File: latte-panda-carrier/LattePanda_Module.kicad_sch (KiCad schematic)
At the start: 9 parts

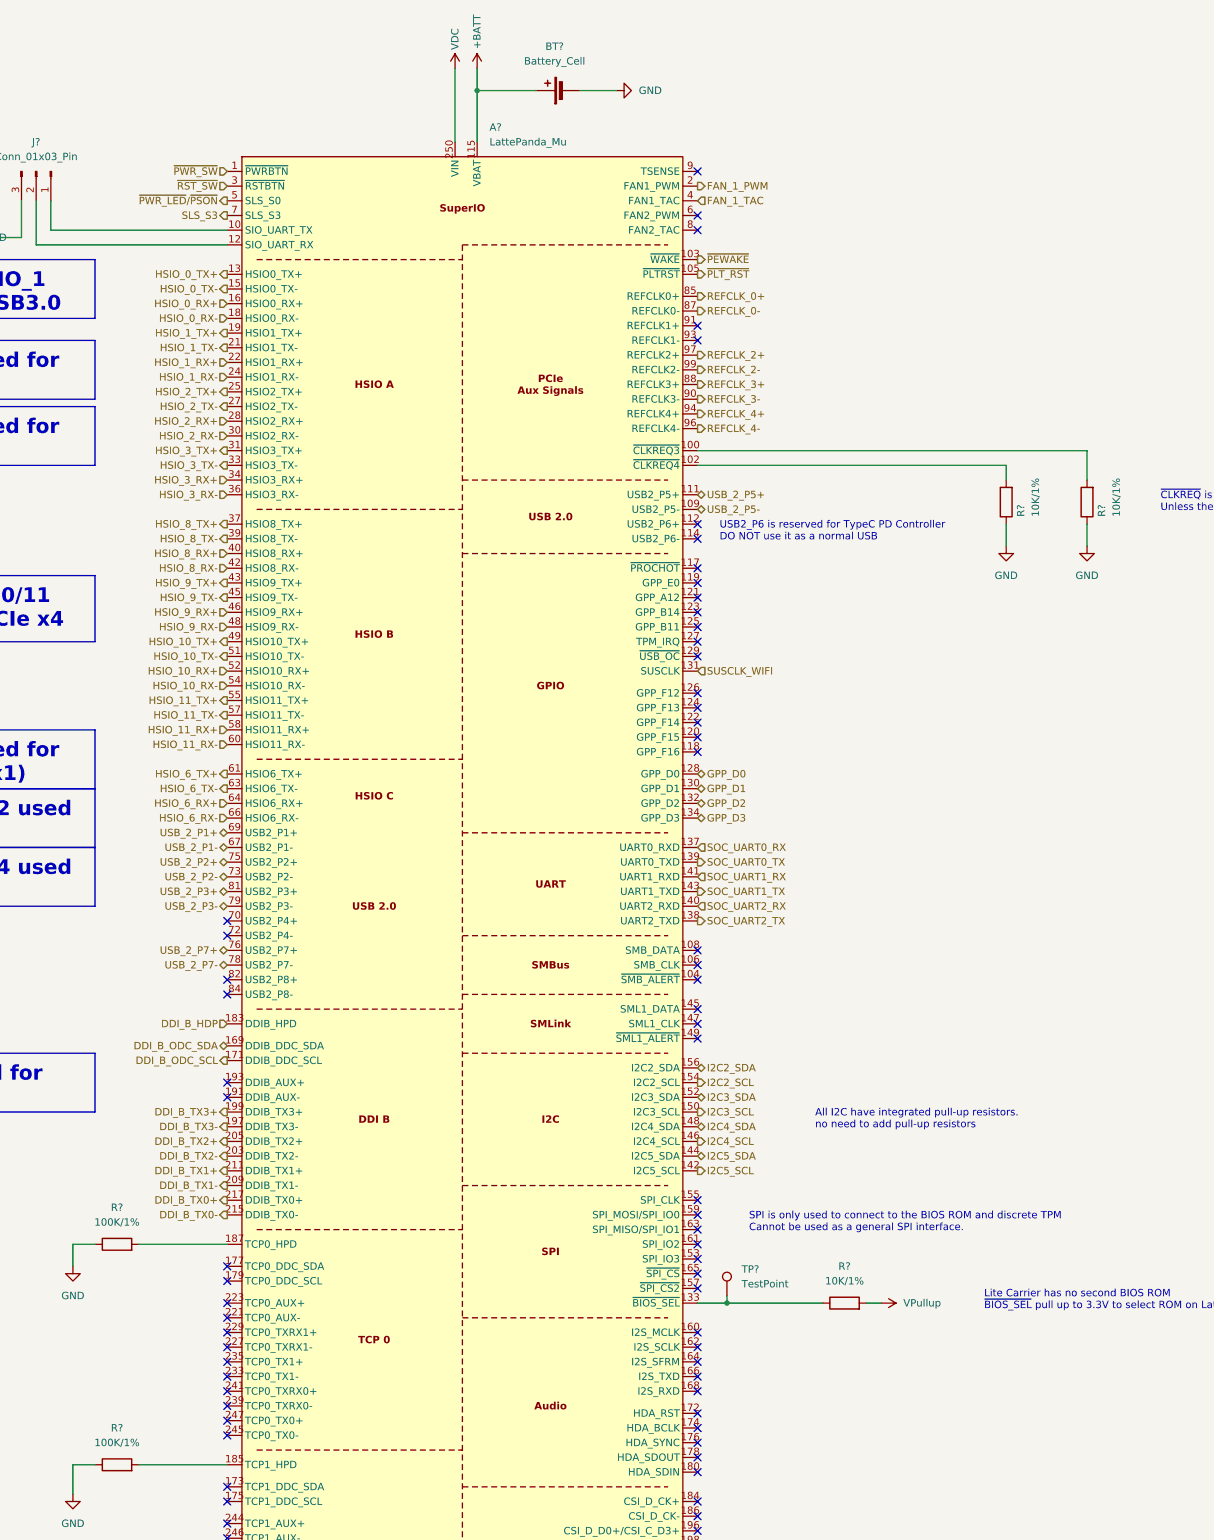
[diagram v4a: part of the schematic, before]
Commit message: 110.3
USB-C sub-circuit
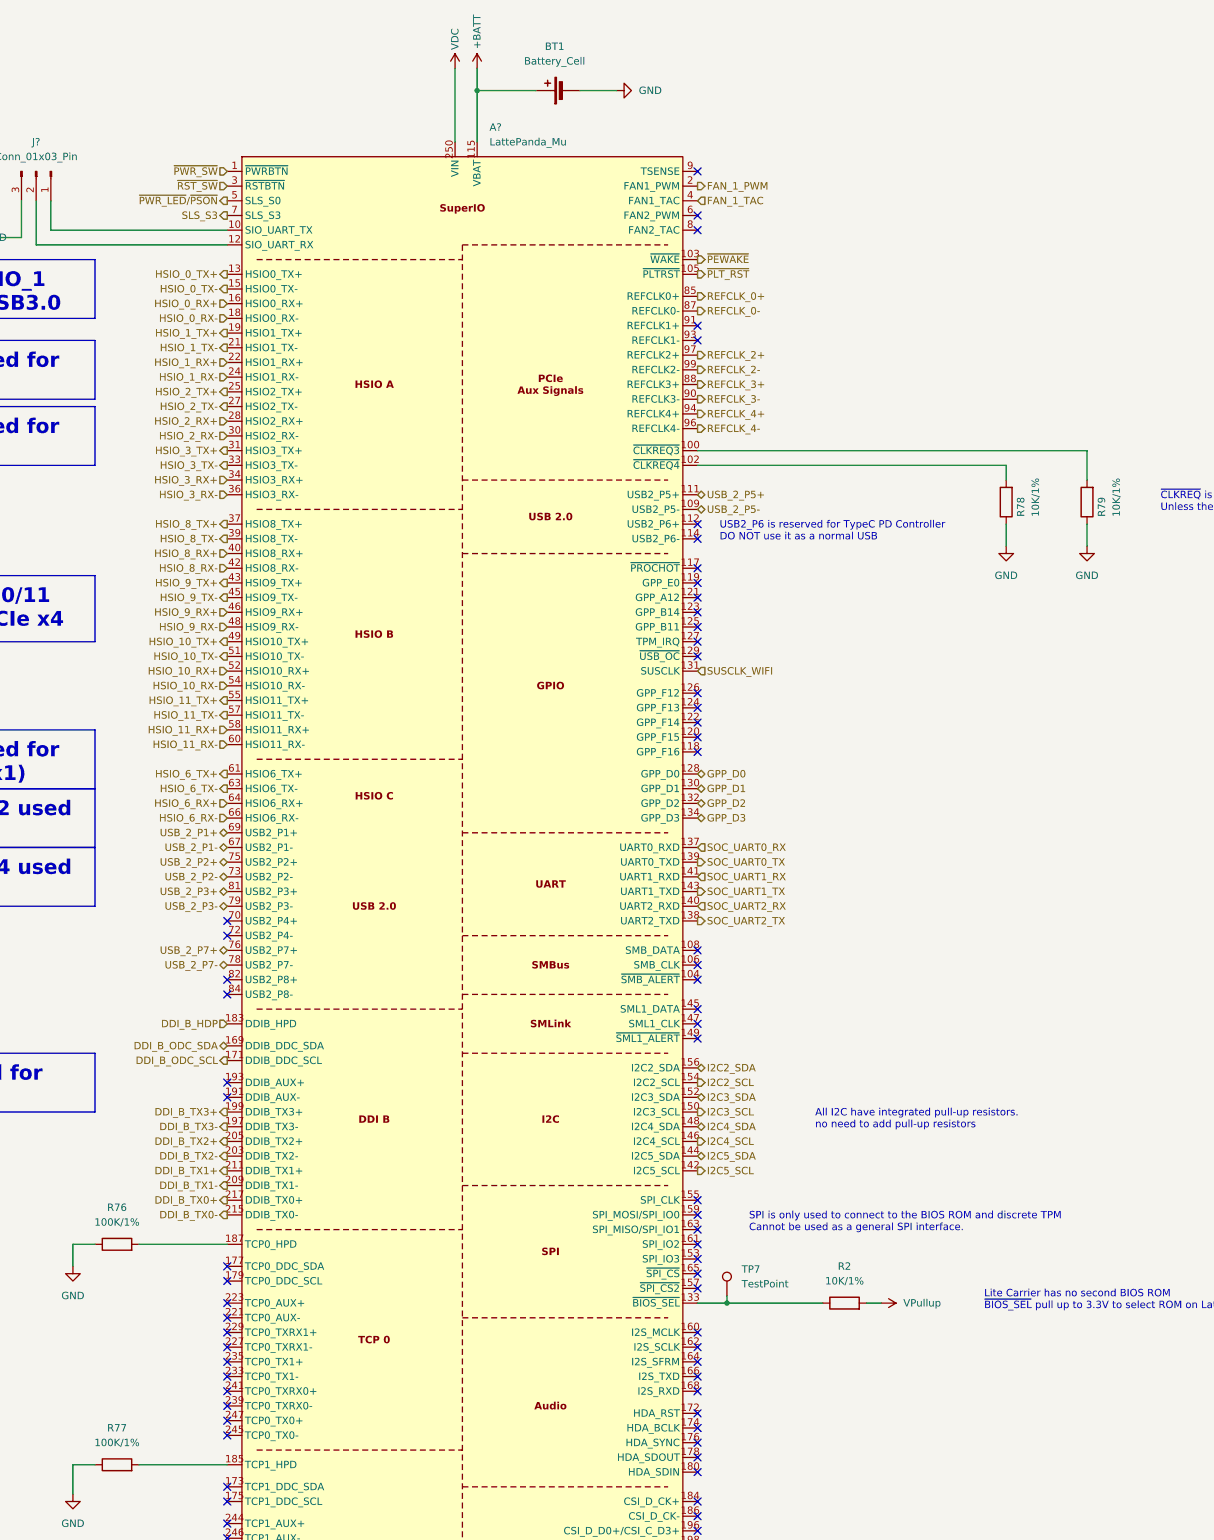
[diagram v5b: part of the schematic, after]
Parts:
- gave numbers to parts that had none: 7
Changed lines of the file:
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@@
 		(on_board yes)
 		(dnp no)
-		(property "Reference" "#PWR?"
+		(property "Reference" "#PWR012"
 			(at 288.29 60.96 0)
 			(effects
@@
 		(dnp no)
 		(fields_autoplaced yes)
-		(property "Reference" "BT?"
+		(property "Reference" "BT1"
 			(at 301.6885 53.34 90)
 			(effects
@@
 		(dnp no)
 		(fields_autoplaced yes)
-		(property "Reference" "TP?"
+		(property "Reference" "TP7"
 			(at 334.01 264.6679 0)
 			(effects
@@
 		(dnp no)
 		(fields_autoplaced yes)
-		(property "Reference" "R?"
+		(property "Reference" "R2"
 			(at 351.79 264.16 90)
 			(effects
@@
 		(dnp no)
 		(fields_autoplaced yes)
-		(property "Reference" "R?"
+		(property "Reference" "R77"
 			(at 226.06 292.1 90)
 			(effects
@@
 		(dnp no)
 		(fields_autoplaced yes)
-		(property "Reference" "#PWR?"
+		(property "Reference" "#PWR010"
 			(at 218.44 309.88 0)
 			(effects
@@
 		(on_board yes)
 		(dnp no)
-		(property "Reference" "R?"
+		(property "Reference" "R78"
 			(at 382.27 134.62 90)
 			(effects
@@
 		(dnp no)
 		(fields_autoplaced yes)
-		(property "Reference" "R?"
+		(property "Reference" "R76"
 			(at 226.06 254 90)
 			(effects
@@
 		(on_board yes)
 		(dnp no)
-		(property "Reference" "#PWR?"
+		(property "Reference" "#PWR011"
 			(at 284.48 60.96 0)
 			(effects
@@
 		(dnp no)
 		(fields_autoplaced yes)
-		(property "Reference" "#PWR?"
+		(property "Reference" "#PWR07"
 			(at 379.73 146.05 0)
 			(effects
@@
 		(dnp no)
 		(fields_autoplaced yes)
-		(property "Reference" "#PWR?"
+		(property "Reference" "#PWR09"
 			(at 218.44 270.51 0)
 			(effects
@@
 		(dnp no)
 		(fields_autoplaced yes)
-		(property "Reference" "#PWR?"
+		(property "Reference" "#PWR05"
 			(at 285.75 354.33 0)
 			(effects
@@
 		(dnp no)
 		(fields_autoplaced yes)
-		(property "Reference" "#PWR?"
+		(property "Reference" "#PWR06"
 			(at 354.33 270.51 0)
 			(effects
@@
 		(dnp no)
 		(fields_autoplaced yes)
-		(property "Reference" "#PWR?"
+		(property "Reference" "#PWR013"
 			(at 318.77 60.96 0)
 			(effects
@@
 		(on_board yes)
 		(dnp no)
-		(property "Reference" "R?"
+		(property "Reference" "R79"
 			(at 396.24 134.62 90)
 			(effects
@@
 		(dnp no)
 		(fields_autoplaced yes)
-		(property "Reference" "#PWR?"
+		(property "Reference" "#PWR08"
 			(at 393.7 146.05 0)
 			(effects
@@
 		(on_board yes)
 		(dnp no)
-		(property "Reference" "#PWR?"
+		(property "Reference" "#PWR014"
 			(at 196.85 86.36 0)
 			(effects

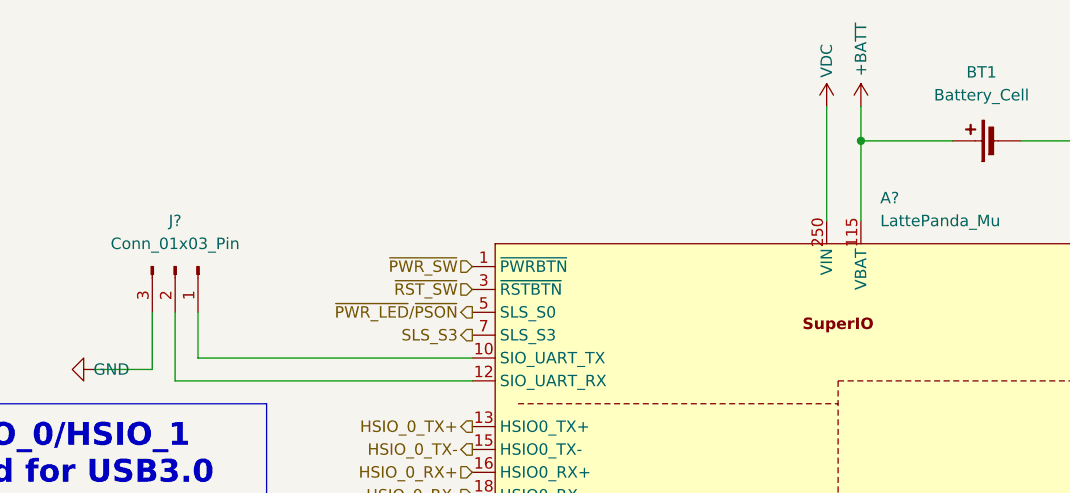
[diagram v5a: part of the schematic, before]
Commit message: Fix missing labels and a few wires
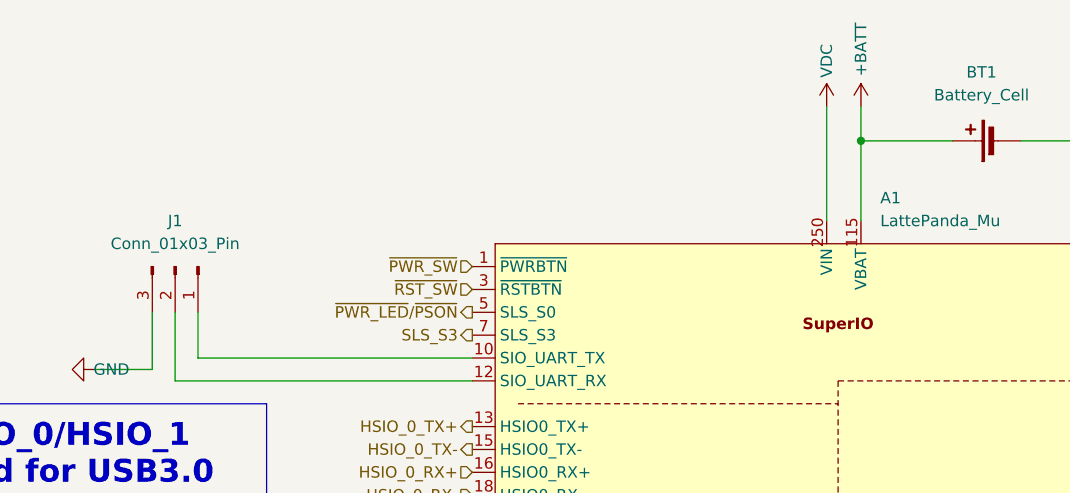
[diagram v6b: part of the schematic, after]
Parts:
- gave numbers to parts that had none: 2
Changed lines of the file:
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@@
 		(dnp no)
 		(fields_autoplaced yes)
-		(property "Reference" "J?"
+		(property "Reference" "J1"
 			(at 212.09 69.85 90)
 			(effects
@@
 			(project ""
 				(path "/9ba2df7d-1c0f-41ea-bb38-2c3f31e14521/b21888af-f6e8-4fba-8e9d-8ac96a3e6368"
-					(reference "J?")
+					(reference "J1")
 					(unit 1)
 				)
@@
 		(dnp no)
 		(fields_autoplaced yes)
-		(property "Reference" "A?"
+		(property "Reference" "A1"
 			(at 290.4333 67.31 0)
 			(effects
@@
 			(project ""
 				(path "/9ba2df7d-1c0f-41ea-bb38-2c3f31e14521/b21888af-f6e8-4fba-8e9d-8ac96a3e6368"
-					(reference "A?")
-					(unit 1)
-				)
+					(reference "A1")
+					(unit 1)
+				)

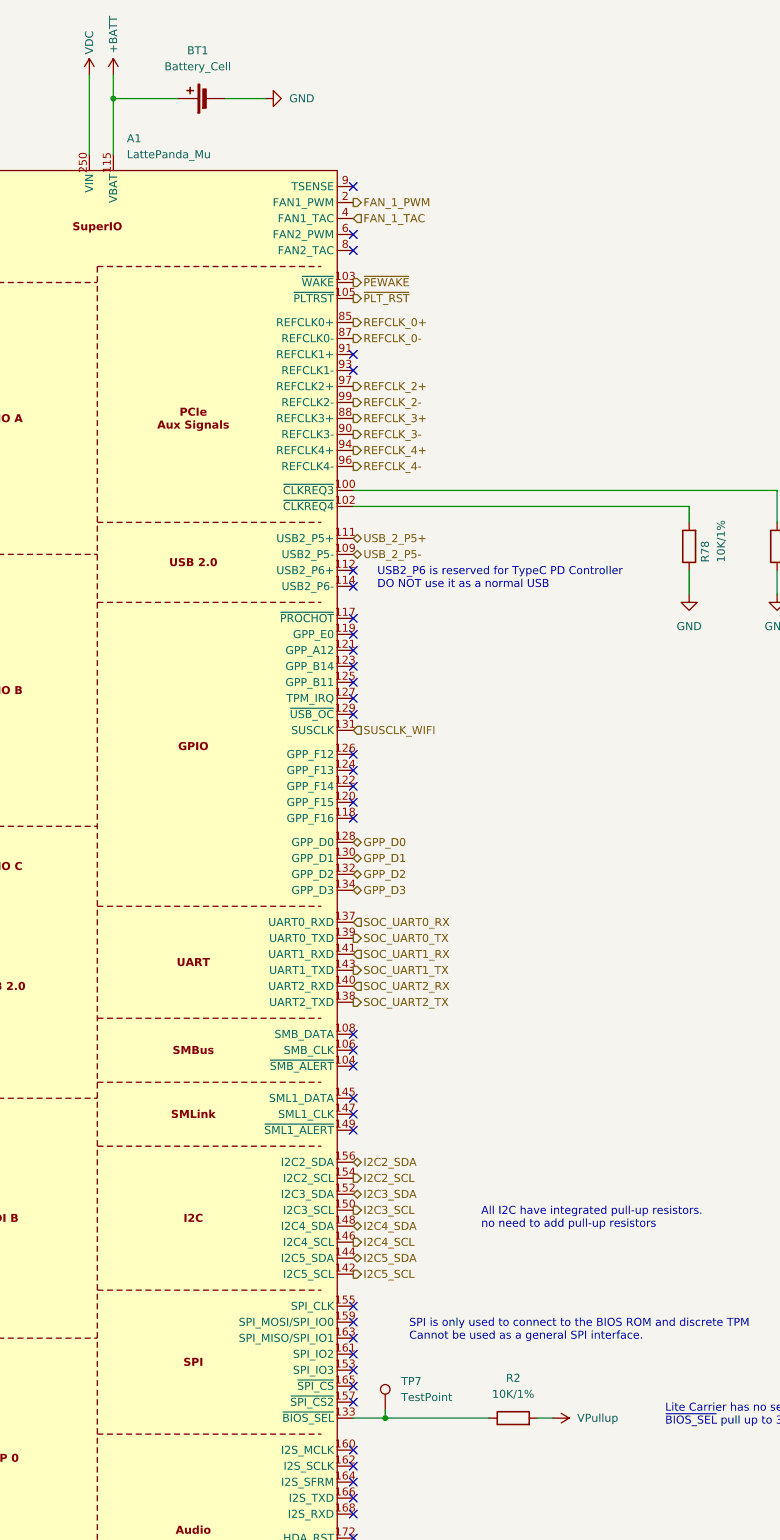
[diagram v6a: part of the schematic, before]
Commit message: Connected sheet pins for PSU through root sheet
Changed not connected pin errors to warnings and also cleared rest of the
errors.
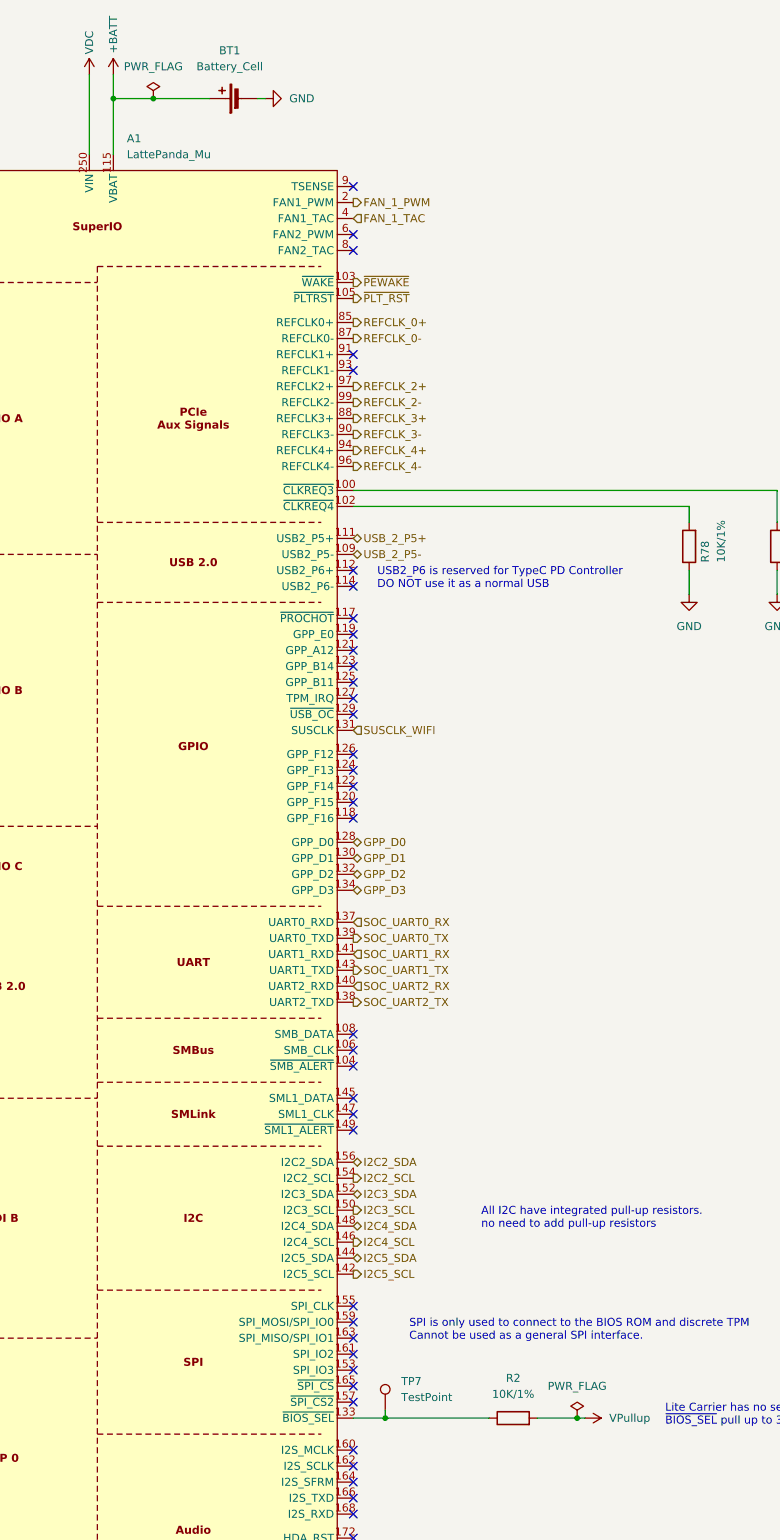
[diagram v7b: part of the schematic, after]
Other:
- moved on the sheet: BT1
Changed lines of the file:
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@@
 		(color 0 0 0 0)
 	)
+	(junction
+		(at 294.64 60.96)
+		(diameter 0)
+		(color 0 0 0 0)
+	)
+	(junction
+		(at 361.95 270.51)
+		(diameter 0)
+		(color 0 0 0 0)
+	)
 	(no_connect
 		(at 245.11 288.29)
@@
 	(wire
 		(pts
+			(xy 294.64 60.96) (xy 303.53 60.96)
+		)
+		(stroke
+			(width 0)
+			(type default)
+		)
+	)
+	(wire
+		(pts
 			(xy 212.09 87.63) (xy 212.09 80.01)
 		)
@@
 	(wire
 		(pts
-			(xy 306.07 60.96) (xy 312.42 60.96)
+			(xy 311.15 60.96) (xy 312.42 60.96)
 		)
 		(stroke
@@
 	(wire
 		(pts
-			(xy 355.6 270.51) (xy 358.14 270.51)
+			(xy 355.6 270.51) (xy 361.95 270.51)
 		)
 		(stroke
@@
 	(wire
 		(pts
-			(xy 288.29 60.96) (xy 298.45 60.96)
+			(xy 288.29 60.96) (xy 294.64 60.96)
 		)
 		(stroke
@@
 	(wire
 		(pts
+			(xy 361.95 270.51) (xy 363.22 270.51)
+		)
+		(stroke
+			(width 0)
+			(type default)
+		)
+	)
+	(wire
+		(pts
 			(xy 229.87 298.45) (xy 245.11 298.45)
 		)
@@
 	(symbol
 		(lib_id "Device:Battery_Cell")
-		(at 303.53 60.96 90)
+		(at 308.61 60.96 90)
 		(unit 1)
 		(exclude_from_sim no)
@@
 		(fields_autoplaced yes)
 		(property "Reference" "BT1"
-			(at 301.6885 53.34 90)
+			(at 306.7685 53.34 90)
 			(effects
 				(font
@@
 		)
 		(property "Value" "Battery_Cell"
-			(at 301.6885 55.88 90)
+			(at 306.7685 55.88 90)
 			(effects
 				(font
@@
 		)
 		(property "Footprint" ""
-			(at 302.006 60.96 90)
+			(at 307.086 60.96 90)
 			(effects
 				(font
@@
 		)
 		(property "Datasheet" "~"
-			(at 302.006 60.96 90)
+			(at 307.086 60.96 90)
 			(effects
 				(font
@@
 		)
 		(property "Description" "Single-cell battery"
-			(at 303.53 60.96 0)
+			(at 308.61 60.96 0)
 			(effects
 				(font
@@
 	)
 	(symbol
+		(lib_id "power:PWR_FLAG")
+		(at 294.64 60.96 0)
+		(unit 1)
+		(exclude_from_sim no)
+		(in_bom yes)
+		(on_board yes)
+		(dnp no)
+		(fields_autoplaced yes)
+		(property "Reference" "#FLG09"
+			(at 294.64 59.055 0)
+			(effects
+				(font
+					(size 1.27 1.27)
+				)
+				(hide yes)
+			)
+		)
+		(property "Value" "PWR_FLAG"
+			(at 294.64 55.88 0)
+			(effects
+				(font
+					(size 1.27 1.27)
+				)
+			)
+		)
+		(property "Footprint" ""
+			(at 294.64 60.96 0)
+			(effects
+				(font
+					(size 1.27 1.27)
+				)
+				(hide yes)
+			)
+		)
+		(property "Datasheet" "~"
+			(at 294.64 60.96 0)
+			(effects
+				(font
+					(size 1.27 1.27)
+				)
+				(hide yes)
+			)
+		)
+		(property "Description" "Special symbol for telling ERC where power comes from"
+			(at 294.64 60.96 0)
+			(effects
+				(font
+					(size 1.27 1.27)
+				)
+				(hide yes)
+			)
+		)
+		(pin "1"
+		)
+		(instances
+			(project ""
+				(path "/9ba2df7d-1c0f-41ea-bb38-2c3f31e14521/b21888af-f6e8-4fba-8e9d-8ac96a3e6368"
+					(reference "#FLG09")
+					(unit 1)
+				)
+			)
+		)
+	)
+	(symbol
 		(lib_id "Device:R")
 		(at 226.06 298.45 90)
@@
 	)
 	(symbol
+		(lib_id "power:PWR_FLAG")
+		(at 361.95 270.51 0)
+		(unit 1)
+		(exclude_from_sim no)
+		(in_bom yes)
+		(on_board yes)
+		(dnp no)
+		(fields_autoplaced yes)
+		(property "Reference" "#FLG010"
+			(at 361.95 268.605 0)
+			(effects
+				(font
+					(size 1.27 1.27)
+				)
+				(hide yes)
+			)
+		)
+		(property "Value" "PWR_FLAG"
+			(at 361.95 265.43 0)
+			(effects
+				(font
+					(size 1.27 1.27)
+				)
+			)
+		)
+		(property "Footprint" ""
+			(at 361.95 270.51 0)
+			(effects
+				(font
+					(size 1.27 1.27)
+				)
+				(hide yes)
+			)
+		)
+		(property "Datasheet" "~"
+			(at 361.95 270.51 0)
+			(effects
+				(font
+					(size 1.27 1.27)
+				)
+				(hide yes)
+			)
+		)
+		(property "Description" "Special symbol for telling ERC where power comes from"
+			(at 361.95 270.51 0)
+			(effects
+				(font
+					(size 1.27 1.27)
+				)
+				(hide yes)
+			)
+		)
+		(pin "1"
+		)
+		(instances
+			(project ""
+				(path "/9ba2df7d-1c0f-41ea-bb38-2c3f31e14521/b21888af-f6e8-4fba-8e9d-8ac96a3e6368"
+					(reference "#FLG010")
+					(unit 1)
+				)
+			)
+		)
+	)
+	(symbol
 		(lib_id "power:VDC")
 		(at 284.48 57.15 0)
@@
 	(symbol
 		(lib_id "power:+3.3V")
-		(at 358.14 270.51 270)
+		(at 363.22 270.51 270)
 		(unit 1)
 		(exclude_from_sim no)
@@
 		(fields_autoplaced yes)
 		(property "Reference" "#PWR06"
-			(at 354.33 270.51 0)
+			(at 359.41 270.51 0)
 			(effects
 				(font
@@
 		)
 		(property "Value" "VPullup"
-			(at 361.95 270.5099 90)
+			(at 367.03 270.5099 90)
 			(effects
 				(font
@@
 		)
 		(property "Footprint" ""
-			(at 358.14 270.51 0)
+			(at 363.22 270.51 0)
 			(effects
 				(font
@@
 		)
 		(property "Datasheet" ""
-			(at 358.14 270.51 0)
+			(at 363.22 270.51 0)
 			(effects
 				(font
@@
 		)
 		(property "Description" "Power symbol creates a global label with name \"VPullup\""
-			(at 358.14 270.51 0)
+			(at 363.22 270.51 0)
 			(effects
 				(font
